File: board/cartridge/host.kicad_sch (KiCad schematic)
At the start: 21 parts, among them P1 Card Edge, U1 74LVC245, U2 NAU8814Y, U4 74LVC245, U5 74LVC245, U8 TXS0108EPW, U9 PCM1754DBQ

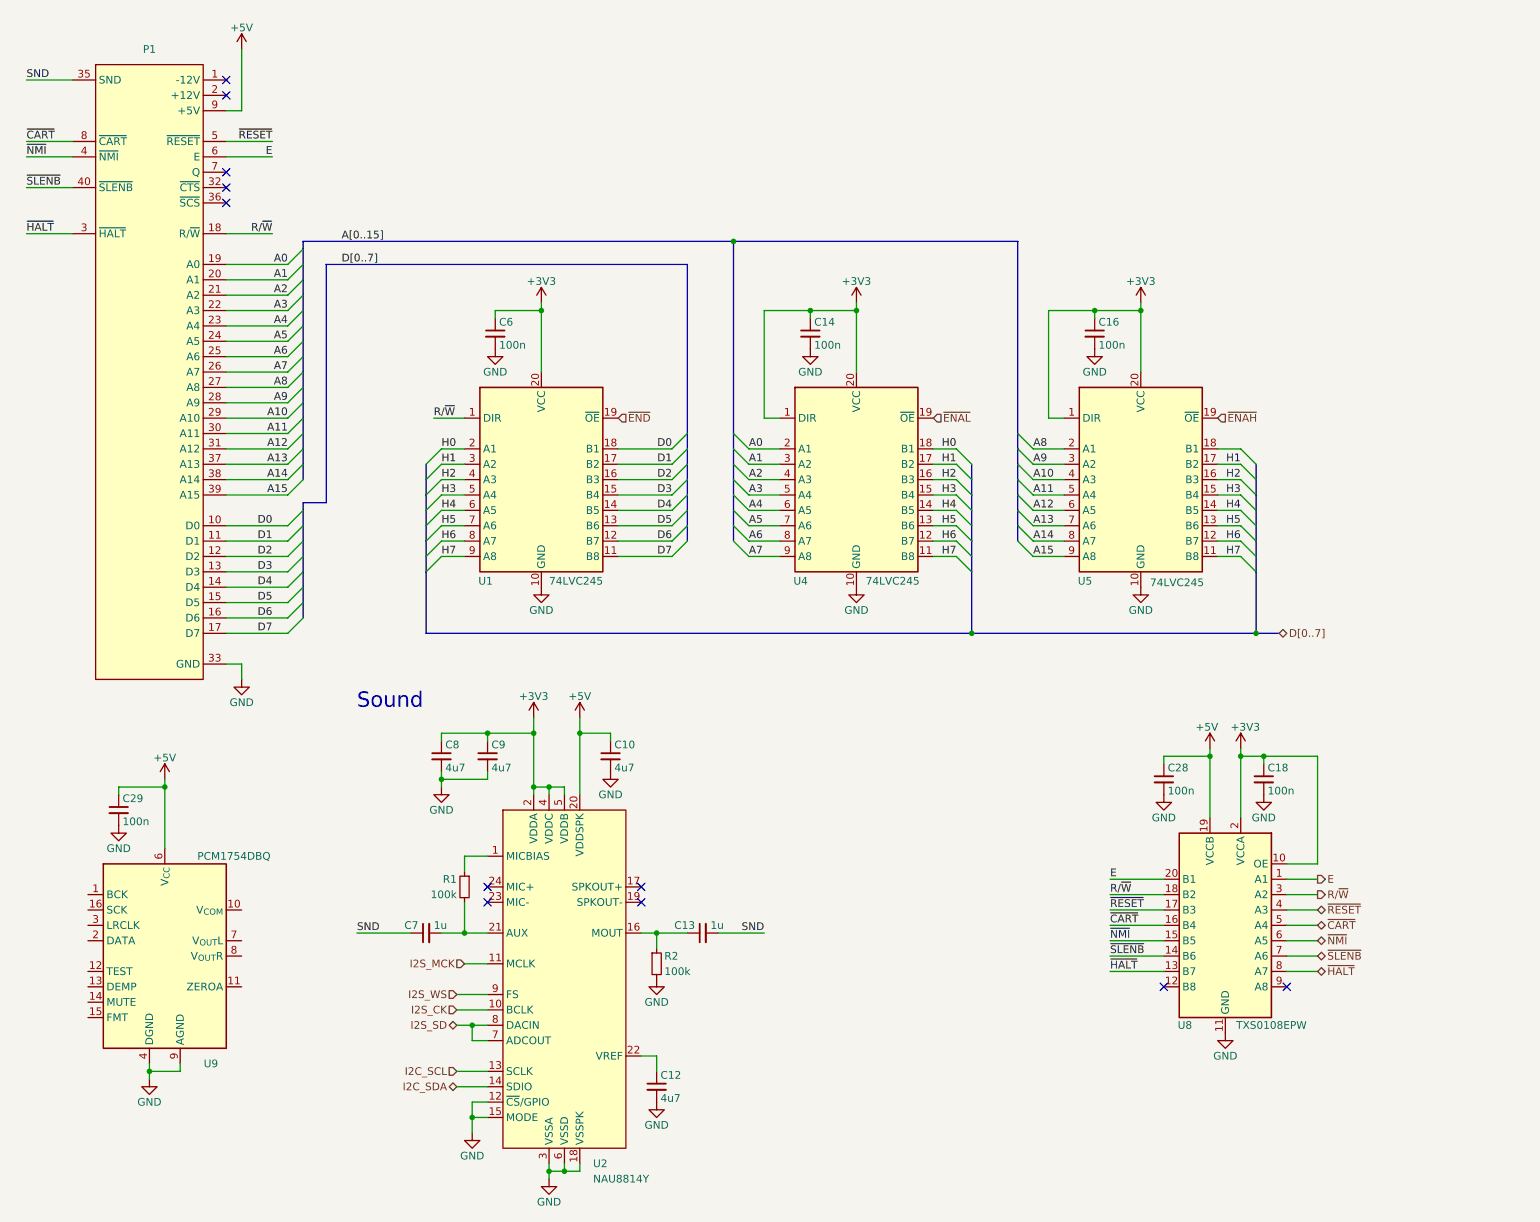
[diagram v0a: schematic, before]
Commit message: Start updating board to use ESP32-S3.
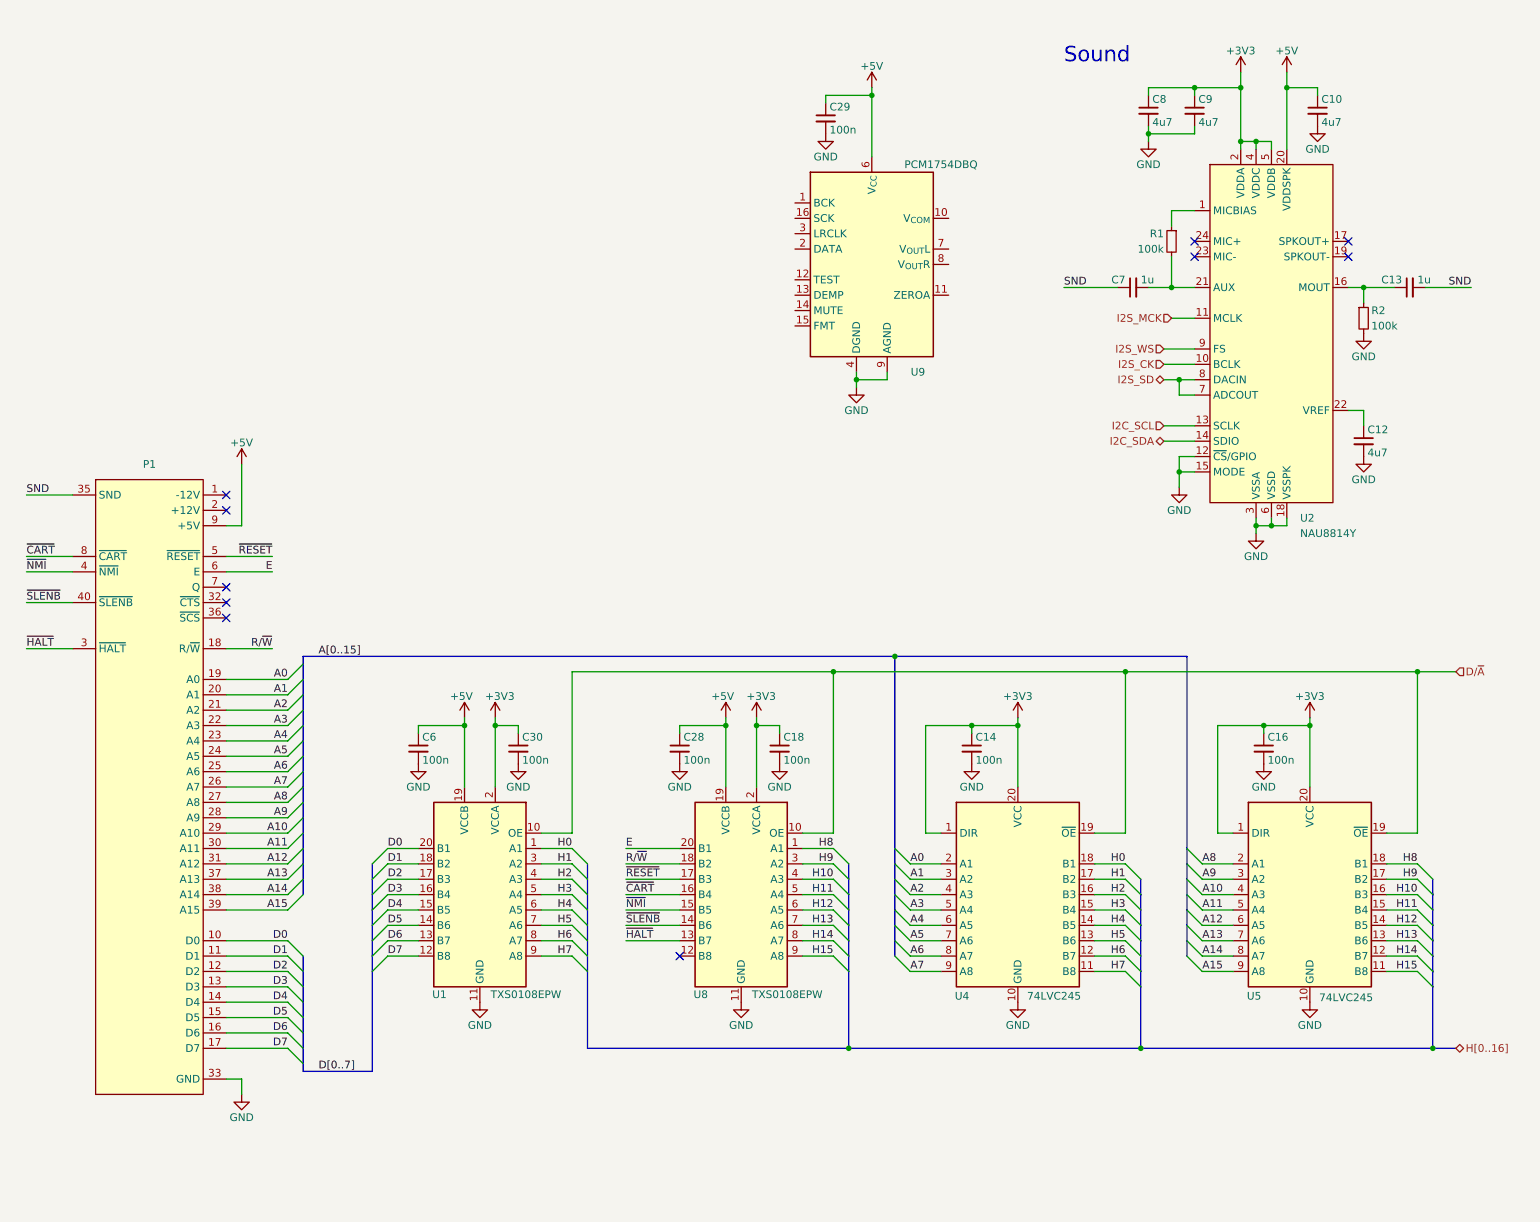
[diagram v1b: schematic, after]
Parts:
- removed U1: 74LVC245, Package_SO:TSSOP-20_4.4x6.5mm_P0.65mm, symbol Logic_LevelTranslator:SN74LVC245APW
- added C30: 100n, Capacitor_SMD:C_0603_1608Metric, symbol Device:C_Small
- added U1: TXS0108EPW, Package_SO:TSSOP-20_4.4x6.5mm_P0.65mm, symbol Logic_LevelTranslator:TXS0108EPW
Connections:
- net ~{ENAL} is gone; now on net D/~{A}: U4.19 (~{OE})
- net +3V3: now also C30.1, U1.2 (VCCA); no longer C6.1, U8.10 (OE)
- net +5V: now also C6.1, U1.19 (VCCB)
- net D0: now also U1.20 (B1)
- net D1: now also U1.18 (B2)
- net D2: now also U1.17 (B3)
- net D3: now also U1.16 (B4)
- net D4: now also U1.15 (B5)
- net D5: now also U1.14 (B6)
- net D6: now also U1.13 (B7)
- net D7: now also U1.12 (B8)
- net E: no longer U8.1 (A1)
- net GND: now also C30.2, U1.11 (GND)
- net H0: now also U1.1 (A1)
- net H1: now also U1.3 (A2); no longer U5.17 (B2)
- net H2: now also U1.4 (A3); no longer U5.16 (B3)
- net H3: now also U1.5 (A4); no longer U5.15 (B4)
- net H4: now also U1.6 (A5); no longer U5.14 (B5)
- net H5: now also U1.7 (A6); no longer U5.13 (B6)
- net H6: now also U1.8 (A7); no longer U5.12 (B7)
- net H7: now also U1.9 (A8); no longer U5.11 (B8)
- net R/~{W}: no longer U8.3 (A2)
- net ~{CART}: no longer U8.5 (A4)
- net ~{HALT}: no longer U8.8 (A7)
- net ~{NMI}: no longer U8.6 (A5)
- net ~{RESET}: no longer U8.4 (A3)
- net ~{SLENB}: no longer U8.7 (A6)
- net H15: now reaches U8.9 (A8)
- net H15: now also U5.11 (B8)
- net H8: now reaches U5.18 (B1)
- net H8: now also U8.1 (A1)
- net ~{ENAH} renamed D/~{A}
- net D/~{A}: now also U8.10 (OE), U1.10 (OE)
- new net H10: U5.16 (B3), U8.4 (A3)
- new net H11: U5.15 (B4), U8.5 (A4)
- new net H12: U5.14 (B5), U8.6 (A5)
- new net H13: U5.13 (B6), U8.7 (A6)
- new net H14: U5.12 (B7), U8.8 (A7)
- new net H9: U5.17 (B2), U8.3 (A2)
- no-connect marks 11 -> 10
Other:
- moved on the sheet: C10, C12, C13, C14, C16, C18, C28, C29, C7, C8, C9, P1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

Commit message: Design and mostly route level shifters.
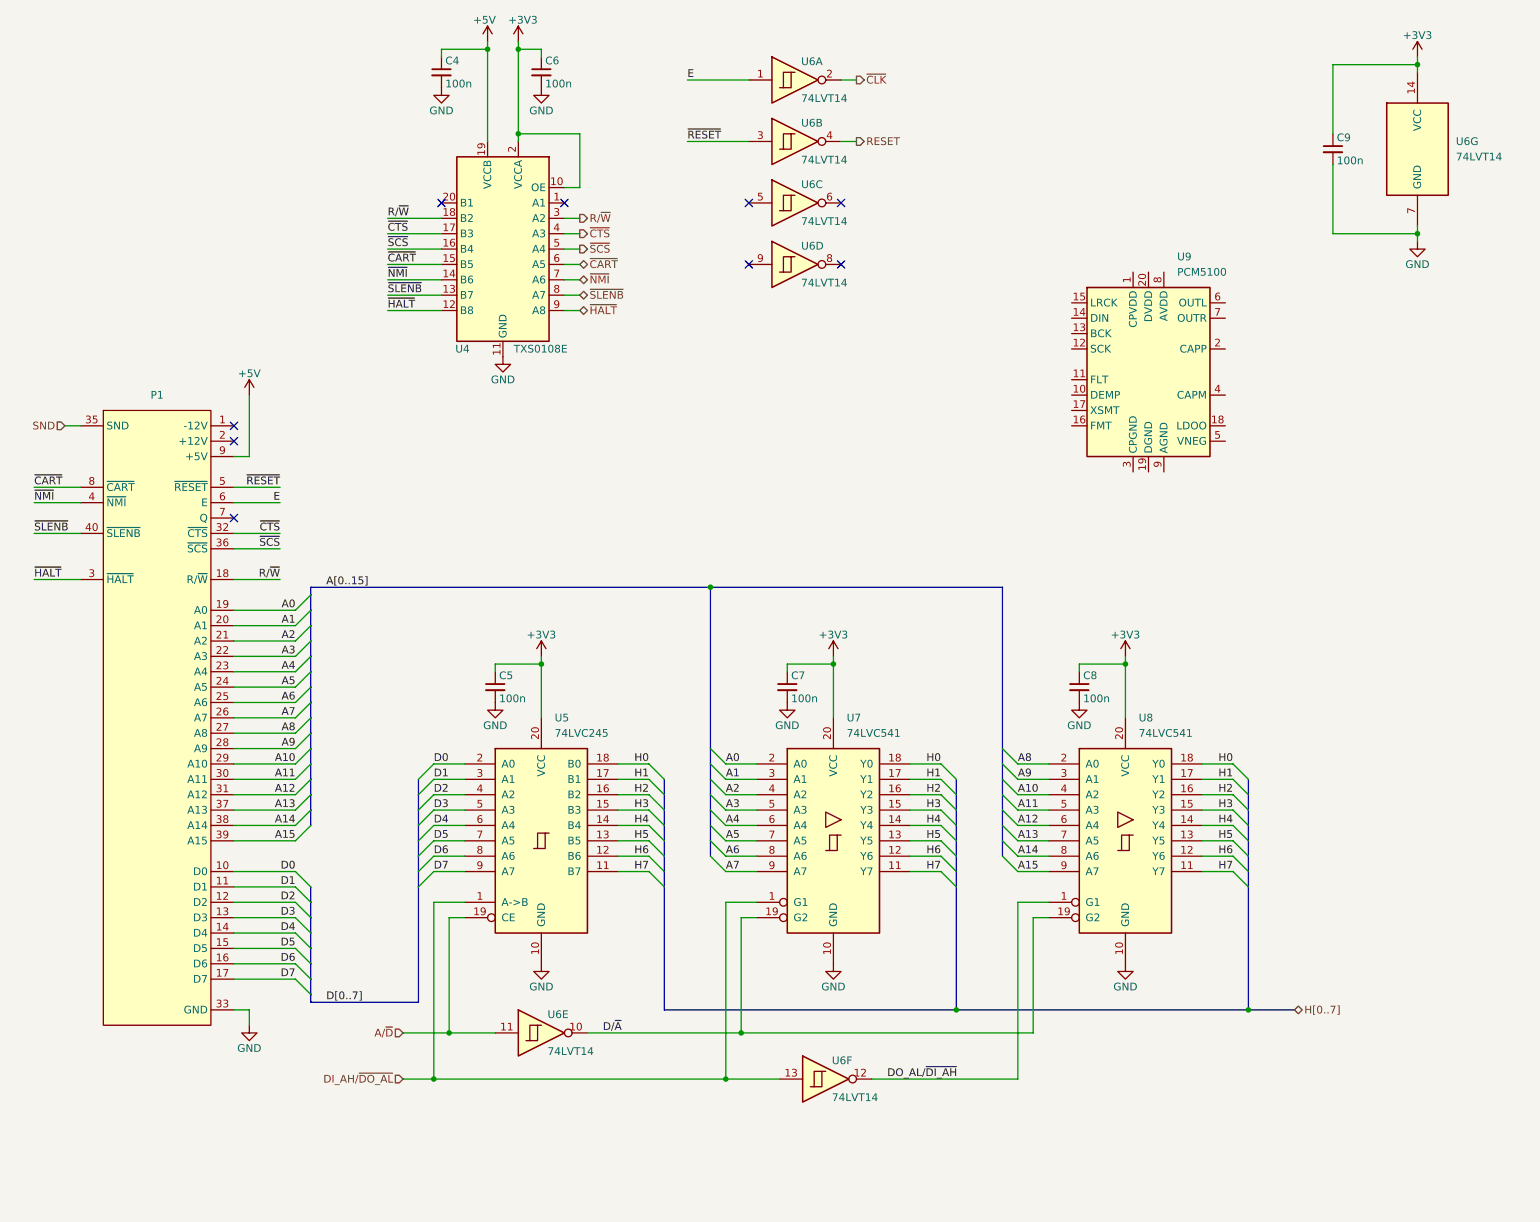
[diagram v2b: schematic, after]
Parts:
- removed C10, C12: 4u7, Capacitor_SMD:C_0603_1608Metric, symbol Device:C_Small
- removed C13: 1u, Capacitor_SMD:C_0603_1608Metric, symbol Device:C_Small
- removed C14, C16, C29, C30, C6: 100n, Capacitor_SMD:C_0603_1608Metric, symbol Device:C_Small
- removed R1, R2: 100k, Resistor_SMD:R_0603_1608Metric, symbol Device:R_Small
- removed U1: TXS0108EPW, Package_SO:TSSOP-20_4.4x6.5mm_P0.65mm, symbol Logic_LevelTranslator:TXS0108EPW
- removed U2: NAU8814Y, Package_DFN_QFN:VQFN-24-1EP_4x4mm_P0.5mm_EP2.5x2.5mm, symbol 0Project:Nuvoton_NAU8814Y
- removed U4, U5: 74LVC245, Package_SO:TSSOP-20_4.4x6.5mm_P0.65mm, symbol Logic_LevelTranslator:SN74LVC245APW
- removed U9: PCM1754DBQ, Package_SO:SSOP-16_3.9x4.9mm_P0.635mm, symbol Audio:PCM1754DBQ
- added C5: 100n, Capacitor_SMD:C_0603_1608Metric, symbol Device:C_Small
- added U5: 74LVC245, Package_SO:TSSOP-20_4.4x6.5mm_P0.65mm, symbol 74xx:74LS245
- added U6: 74LVT14, Package_SO:TSSOP-14_4.4x5mm_P0.65mm, symbol 74xx:74HC14
- added U7, U8: 74LVC541, Package_SO:TSSOP-20_4.4x6.5mm_P0.65mm, symbol 74xx:74LS541
- added U9: PCM5100, Package_SO:TSSOP-20_4.4x6.5mm_P0.65mm, symbol Audio:PCM5100
- C7: value 1u -> 100n
- C8, C9: value 4u7 -> 100n
- U4: renamed from U8; value TXS0108EPW -> TXS0108E
- renumbered C28 to C4, C18 to C6
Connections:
- net H10 is gone; now on net ~{CTS}: U4.4 (A3)
- net H11 is gone; now on net ~{SCS}: U4.5 (A4)
- net H12 is gone; now on net ~{CART}: U4.6 (A5)
- net H13 is gone; now on net ~{NMI}: U4.7 (A6)
- net H14 is gone; now on net ~{SLENB}: U4.8 (A7)
- net H15 is gone; now on net ~{HALT}: U4.9 (A8)
- net H9 is gone; now on net R/~{W}: U4.3 (A2)
- net +3V3: now also C7.1, U4.10 (OE), C5.1, U5.20 (VCC), U6.14 (VCC), U7.20 (VCC), U8.20 (VCC)
- net A0: now also U7.2 (A0)
- net A1: now also U7.3 (A1)
- net A10: now also U8.4 (A2)
- net A11: now also U8.5 (A3)
- net A12: now also U8.6 (A4)
- net A13: now also U8.7 (A5)
- net A14: now also U8.8 (A6)
- net A15: now also U8.9 (A7)
- net A2: now also U7.4 (A2)
- net A3: now also U7.5 (A3)
- net A4: now also U7.6 (A4)
- net A5: now also U7.7 (A5)
- net A6: now also U7.8 (A6)
- net A7: now also U7.9 (A7)
- net A8: now also U8.2 (A0)
- net A9: now also U8.3 (A1)
- net D0: now also U5.2 (A0)
- net D1: now also U5.3 (A1)
- net D2: now also U5.4 (A2)
- net D3: now also U5.5 (A3)
- net D4: now also U5.6 (A4)
- net D5: now also U5.7 (A5)
- net D6: now also U5.8 (A6)
- net D7: now also U5.9 (A7)
- net D/~{A}: now also U6.10, U7.19 (G2), U8.19 (G2); no longer U4.10 (OE)
- net E: now also U6.1; no longer U4.20 (B1)
- net GND: now also C7.2, C5.2, U5.10 (GND), U6.7 (GND), U7.10 (GND), U8.10 (GND)
- net H0: now also U5.18 (B0), U7.18 (Y0), U8.18 (Y0)
- net H1: now also U5.17 (B1), U7.17 (Y1), U8.17 (Y1)
- net H2: now also U5.16 (B2), U7.16 (Y2), U8.16 (Y2)
- net H3: now also U5.15 (B3), U7.15 (Y3), U8.15 (Y3)
- net H4: now also U5.14 (B4), U7.14 (Y4), U8.14 (Y4)
- net H5: now also U5.13 (B5), U7.13 (Y5), U8.13 (Y5)
- net H6: now also U5.12 (B6), U7.12 (Y6), U8.12 (Y6)
- net H7: now also U5.11 (B7), U7.11 (Y7), U8.11 (Y7)
- net SND: no longer C7.1
- net ~{CART}: now also U4.15 (B5); no longer U4.16 (B4)
- net ~{HALT}: now also U4.12 (B8); no longer U4.13 (B7)
- net ~{NMI}: now also U4.14 (B6); no longer U4.15 (B5)
- net ~{RESET}: now also U6.3; no longer U4.17 (B3)
- net ~{SLENB}: now also U4.13 (B7); no longer U4.14 (B6)
- net ~{CTS}: now reaches P1.32 (~{CTS})
- net ~{CTS}: now also U4.17 (B3)
- net ~{SCS}: now reaches P1.36 (~{SCS})
- net ~{SCS}: now also U4.16 (B4)
- net H8: no longer names the net of U4.1 (A1)
- new net A/~{D}: U5.19 (CE), U6.11
- new net DI_AH/~{DO_AL}: U5.1 (A->B), U6.13, U7.1 (G1)
- new net DO_AL/~{DI_AH}: U6.12, U8.1 (G1)
- new net RESET: U6.4
- new net ~{CLK}: U6.2
- no-connect marks 10 -> 9
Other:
- note removed: "Sound"
- moved on the sheet: C4, C6, P1, U4
